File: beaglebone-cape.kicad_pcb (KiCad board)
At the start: 2 copper layers, 86.4 x 54.6 mm, 9 parts, among them J1 CONN_2X2, P1 BEAGLEBONE_BLACK, U1 24C16

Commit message: Ironed out footprints with Rob, started placing stuff
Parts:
- added C2: 10 uF (25V), Capacitors_ThroughHole:C_Radial_D5_L6_P2.5, F.Cu at (166.4, 123.2)
- added C3: 22 uF (16V), Capacitors_ThroughHole:C_Radial_D5_L6_P2.5, F.Cu at (144.8, 124.5)
- added D1: PWR +12V, LEDs:LED-3MM, F.Cu at (222.9, 214.1)
- added D2: PWR +5V, LEDs:LED-3MM, F.Cu at (255.3, 204.5)
- added D3: RED, LEDs:LED-3MM, F.Cu at (230.1, 171.1)
- added D4: GREEN, LEDs:LED-3MM, F.Cu at (226.1, 130.8)
- added D5: RELAY ON, LEDs:LED-3MM, F.Cu at (184.1, 266.7)
- added D6: RELAY ON, LEDs:LED-3MM, F.Cu at (202.3, 258.5)
- added D7: 1N4007, Diodes_ThroughHole:Diode_DO-41_SOD81_Horizontal_RM10, F.Cu at (139.7, 102.9)
- added D8: 1N4007, Diodes_ThroughHole:Diode_DO-41_SOD81_Horizontal_RM10, F.Cu at (139.7, 116.8)
- added D9: 1N4007, Diodes_ThroughHole:Diode_DO-41_SOD81_Horizontal_RM10, F.Cu at (200.8, 225.9)
- added P2: 12V, Terminal_Blocks:TerminalBlock_Pheonix_MPT-2.54mm_2pol, F.Cu at (190.5, 109.2)
- added P3: RED_LIGHT, Terminal_Blocks:TerminalBlock_Pheonix_MPT-2.54mm_2pol, F.Cu at (190.5, 96.5)
- added P4: JUMPERS, Pin_Headers:Pin_Header_Straight_2x02, F.Cu at (176.8, 210.2)
- added P5: GREEN_LIGHT, Terminal_Blocks:TerminalBlock_Pheonix_MPT-2.54mm_2pol, F.Cu at (190.5, 90.2)
- added P6: CONN_01X05, Pin_Headers:Pin_Header_Straight_1x05, F.Cu at (119.4, 105.4)
- added P7: NC/NO JUMPER, Pin_Headers:Pin_Header_Straight_1x03, F.Cu at (179.1, 105.4)
- added P8: NC/NO JUMPER, Pin_Headers:Pin_Header_Straight_1x03, F.Cu at (184.2, 109.2)
- added P9: DOOR STRIKE/MAGNET, Terminal_Blocks:TerminalBlock_Pheonix_MPT-2.54mm_2pol, F.Cu at (190.5, 102.9)
- added Q1: 2N7000, TO_SOT_Packages_THT:TO-92_Inline_Narrow_Oval, F.Cu at (248.2, 190.9)
- added Q2: 2N7000, TO_SOT_Packages_THT:TO-92_Inline_Narrow_Oval, F.Cu at (239.1, 184.8)
- added Q3: 2N7000, TO_SOT_Packages_THT:TO-92_Inline_Narrow_Oval, F.Cu at (216.3, 246.2)
- added Q4: 2N7000, TO_SOT_Packages_THT:TO-92_Inline_Narrow_Oval, F.Cu at (195.4, 259.6)
- added R10: 1k, Resistors_ThroughHole:Resistor_Vertical_RM5mm, F.Cu at (230.9, 194.8)
- added R11: 330, Resistors_ThroughHole:Resistor_Vertical_RM5mm, F.Cu at (196.4, 208.4)
- added R12: 10k, Resistors_ThroughHole:Resistor_Vertical_RM5mm, F.Cu at (186.6, 208.4)
- added R13: 1k, Resistors_ThroughHole:Resistor_Vertical_RM5mm, F.Cu at (241.1, 164.2)
- added R14: 330, Resistors_ThroughHole:Resistor_Vertical_RM5mm, F.Cu at (187.8, 247.2)
- added R15: 330, Resistors_ThroughHole:Resistor_Vertical_RM5mm, F.Cu at (177.0, 259.2)
- added R16: 330, Resistors_ThroughHole:Resistor_Vertical_RM5mm, F.Cu at (167.3, 259.2)
- added R17: 330, Resistors_ThroughHole:Resistor_Vertical_RM5mm, F.Cu at (217.5, 225.6)
- added R18: 10k, Resistors_ThroughHole:Resistor_Vertical_RM5mm, F.Cu at (197.5, 248.9)
- added R19: 10k, Resistors_ThroughHole:Resistor_Vertical_RM5mm, F.Cu at (208.7, 235.6)
- added R20: 1k, Resistors_ThroughHole:Resistor_Vertical_RM5mm, F.Cu at (218.4, 235.6)
- added R21: 1k, Resistors_ThroughHole:Resistor_Vertical_RM5mm, F.Cu at (208.7, 245.5)
- added R22: 2k, Resistors_ThroughHole:Resistor_Vertical_RM5mm, F.Cu at (198.9, 239.0)
- added R23: 2k, Resistors_ThroughHole:Resistor_Vertical_RM5mm, F.Cu at (187.8, 257.2)
- added R6: 1k, Resistors_ThroughHole:Resistor_Vertical_RM5mm, F.Cu at (241.2, 174.1)
- added R7: 330, Resistors_ThroughHole:Resistor_Vertical_RM5mm, F.Cu at (250.9, 160.6)
- added R8: 330, Resistors_ThroughHole:Resistor_Vertical_RM5mm, F.Cu at (250.9, 170.5)
- added R9: 10k, Resistors_ThroughHole:Resistor_Vertical_RM5mm, F.Cu at (206.1, 208.4)
- added RLY1: JW2SN-DC5V, panasonic_jw:Panasonic_JW, F.Cu at (158.8, 97.8)
- added RLY2: JW2SN-DC5V, panasonic_jw:Panasonic_JW, F.Cu at (158.8, 111.8)
- added SW1: PWR_SWITCH, Buttons_Switches_ThroughHole:SW_PUSH_SMALL, F.Cu at (100.3, 97.8)
- added SW2: RESET_SWITCH, Buttons_Switches_ThroughHole:SW_PUSH_SMALL, F.Cu at (100.3, 90.2)
- added U2: V7805-2000, V78XX:V78XX, F.Cu at (156.2, 125.7)
- added U3: 4N25, Housings_DIP:DIP-6_W7.62mm, F.Cu at (137.2, 100.3)
- added U4: 4N25, Housings_DIP:DIP-6_W7.62mm, F.Cu at (137.2, 113.0)
- C1: value 0.1u -> 0.1uF (25V); footprint SM0805 -> Capacitors_ThroughHole:C_Radial_D5_L6_P2.5
- P1: footprint BEAGLEBONE_BLACK -> beagleboard:BEAGLEBONE_BLACK
- R1, R2, R3: footprint SM0805 -> Resistors_ThroughHole:Resistor_Vertical_RM5mm
- R4, R5: value 1.5k -> 5.6k; footprint SM0805 -> Resistors_ThroughHole:Resistor_Vertical_RM5mm
- U1: value 24C16 -> 24C256; footprint SO8E -> Housings_DIP:DIP-8_W7.62mm
- moved R3 158.8 mm to (259.0, 168.6)
- moved R4 154.6 mm to (259.5, 161.5)
- moved R2 153.3 mm to (256.0, 168.6)
- moved R5 149.1 mm to (256.4, 161.5)
- moved C1 129.2 mm to (227.4, 173.1)
- moved J1 111.8 mm to (212.1, 129.5)
- moved R1 96.0 mm to (156.8, 214.6)
- moved U1 4.45 mm to (100.3, 128.3), turned to 90 degrees
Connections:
- net /DC_3.3V renamed +3V3
- net /VDD_5V renamed +5V
- P1 pad A10: (no net) -> /GPIO_68
- P1 pad A11: (no net) -> /GPIO_45
- P1 pad A12: (no net) -> /GPIO_44
- P1 pad A13: (no net) -> /EHRPWM2B
- P1 pad A14: (no net) -> /GPIO_26
- P1 pad A15: (no net) -> /LOCK_RELAYS/R1_ENGAGE
- P1 pad A16: (no net) -> /LOCK_RELAYS/R1_READ
- P1 pad A17: (no net) -> /LOCK_RELAYS/R2_ENGAGE
- P1 pad A18: (no net) -> /LOCK_RELAYS/R2_READ
- P1 pad A19: (no net) -> /EHRPWM2A
- P1 pad A20: (no net) -> /MMC1_CMD
- P1 pad A21: (no net) -> /MMC1_CLK
- P1 pad A22: (no net) -> /MMC1_DAT5
- P1 pad A23: (no net) -> /MMC1_DAT4
- P1 pad A24: (no net) -> /MMC1_DAT1
- P1 pad A25: (no net) -> /MMC1_DAT0
- P1 pad A26: (no net) -> /GPIO_61
- P1 pad A27: (no net) -> /LCD_VSYNC
- P1 pad A28: (no net) -> /LCD_PCLK
- P1 pad A29: (no net) -> /LCD_HSYNC
- P1 pad A3: (no net) -> /MMC1_DAT6
- P1 pad A30: (no net) -> /LCD_AC_BIAS
- P1 pad A31: (no net) -> /LCD_DATA14
- P1 pad A32: (no net) -> /LCD_DATA15
- P1 pad A33: (no net) -> /LCD_DATA13
- P1 pad A34: (no net) -> /LCD_DATA11
- P1 pad A35: (no net) -> /LCD_DATA12
- P1 pad A36: (no net) -> /LCD_DATA10
- P1 pad A37: (no net) -> /LCD_DATA8
- P1 pad A38: (no net) -> /LCD_DATA9
- P1 pad A39: (no net) -> /LCD_DATA6
- P1 pad A4: (no net) -> /MMC1_DAT7
- P1 pad A40: (no net) -> /LCD_DATA7
- P1 pad A41: (no net) -> /LCD_DATA4
- P1 pad A42: (no net) -> /LCD_DATA5
- P1 pad A43: (no net) -> /LCD_DATA2
- P1 pad A44: (no net) -> /LCD_DATA3
- P1 pad A45: (no net) -> /LCD_DATA0
- P1 pad A46: (no net) -> /LCD_DATA1
- P1 pad A5: (no net) -> /MMC1_DAT2
- P1 pad A6: (no net) -> /MMC1_DAT3
- P1 pad A7: (no net) -> /GPIO_66
- P1 pad A8: (no net) -> /GPIO_67
- P1 pad A9: (no net) -> /GPIO_69
- P1 pad B10: (no net) -> /SYS_RESETn
- P1 pad B11: (no net) -> /UART4_RXD
- P1 pad B12: (no net) -> /GPIO_60
- P1 pad B13: (no net) -> /UART4_TXD
- P1 pad B14: (no net) -> /EHRPWM1A
- P1 pad B15: (no net) -> /GPIO_48
- P1 pad B16: (no net) -> /EHRPWM1B
- P1 pad B17: (no net) -> /SPIO_CSO
- P1 pad B18: (no net) -> /SPIO_D1
- P1 pad B21: (no net) -> /SPIO_DO
- P1 pad B22: (no net) -> /SPIO_SLCK
- P1 pad B23: (no net) -> /GPIO_49
- P1 pad B24: (no net) -> /UART1_TXD
- P1 pad B25: (no net) -> /GPIO_117
- P1 pad B26: (no net) -> /UART1_RXD
- P1 pad B27: (no net) -> /GPIO_115
- P1 pad B28: (no net) -> /SPI1_CS0
- P1 pad B29: (no net) -> /SPI1_D0
- P1 pad B30: (no net) -> /GPIO_112
- P1 pad B31: (no net) -> /SPI1_SCLK
- P1 pad B32: (no net) -> /VADC
- P1 pad B33: (no net) -> /AIN4
- P1 pad B34: (no net) -> /AGND
- P1 pad B35: (no net) -> /AIN6
- P1 pad B36: (no net) -> /AIN5
- P1 pad B37: (no net) -> /AIN2
- P1 pad B38: (no net) -> /AIN3
- P1 pad B39: (no net) -> /AIN0
- P1 pad B40: (no net) -> /AIN1
- P1 pad B41: (no net) -> /GPIO_20
- P1 pad B42: (no net) -> /ECAPWMO
- P1 pad B9: (no net) -> /PWR_BUT
- U1 pad 7: (no net) -> Net-(U1-Pad7)
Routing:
- net (no net): track 0.00 -> 51.8 mm, vias 0 -> 2
- net /A0: track 15.6 -> 0.00 mm
- net +3V3: track 43.4 -> 31.1 mm
- net /A2: track 11.2 -> 0.00 mm
- net /A1: track 10.1 -> 0.00 mm
- net GND: track 2.60 -> 0.00 mm, vias 2 -> 0

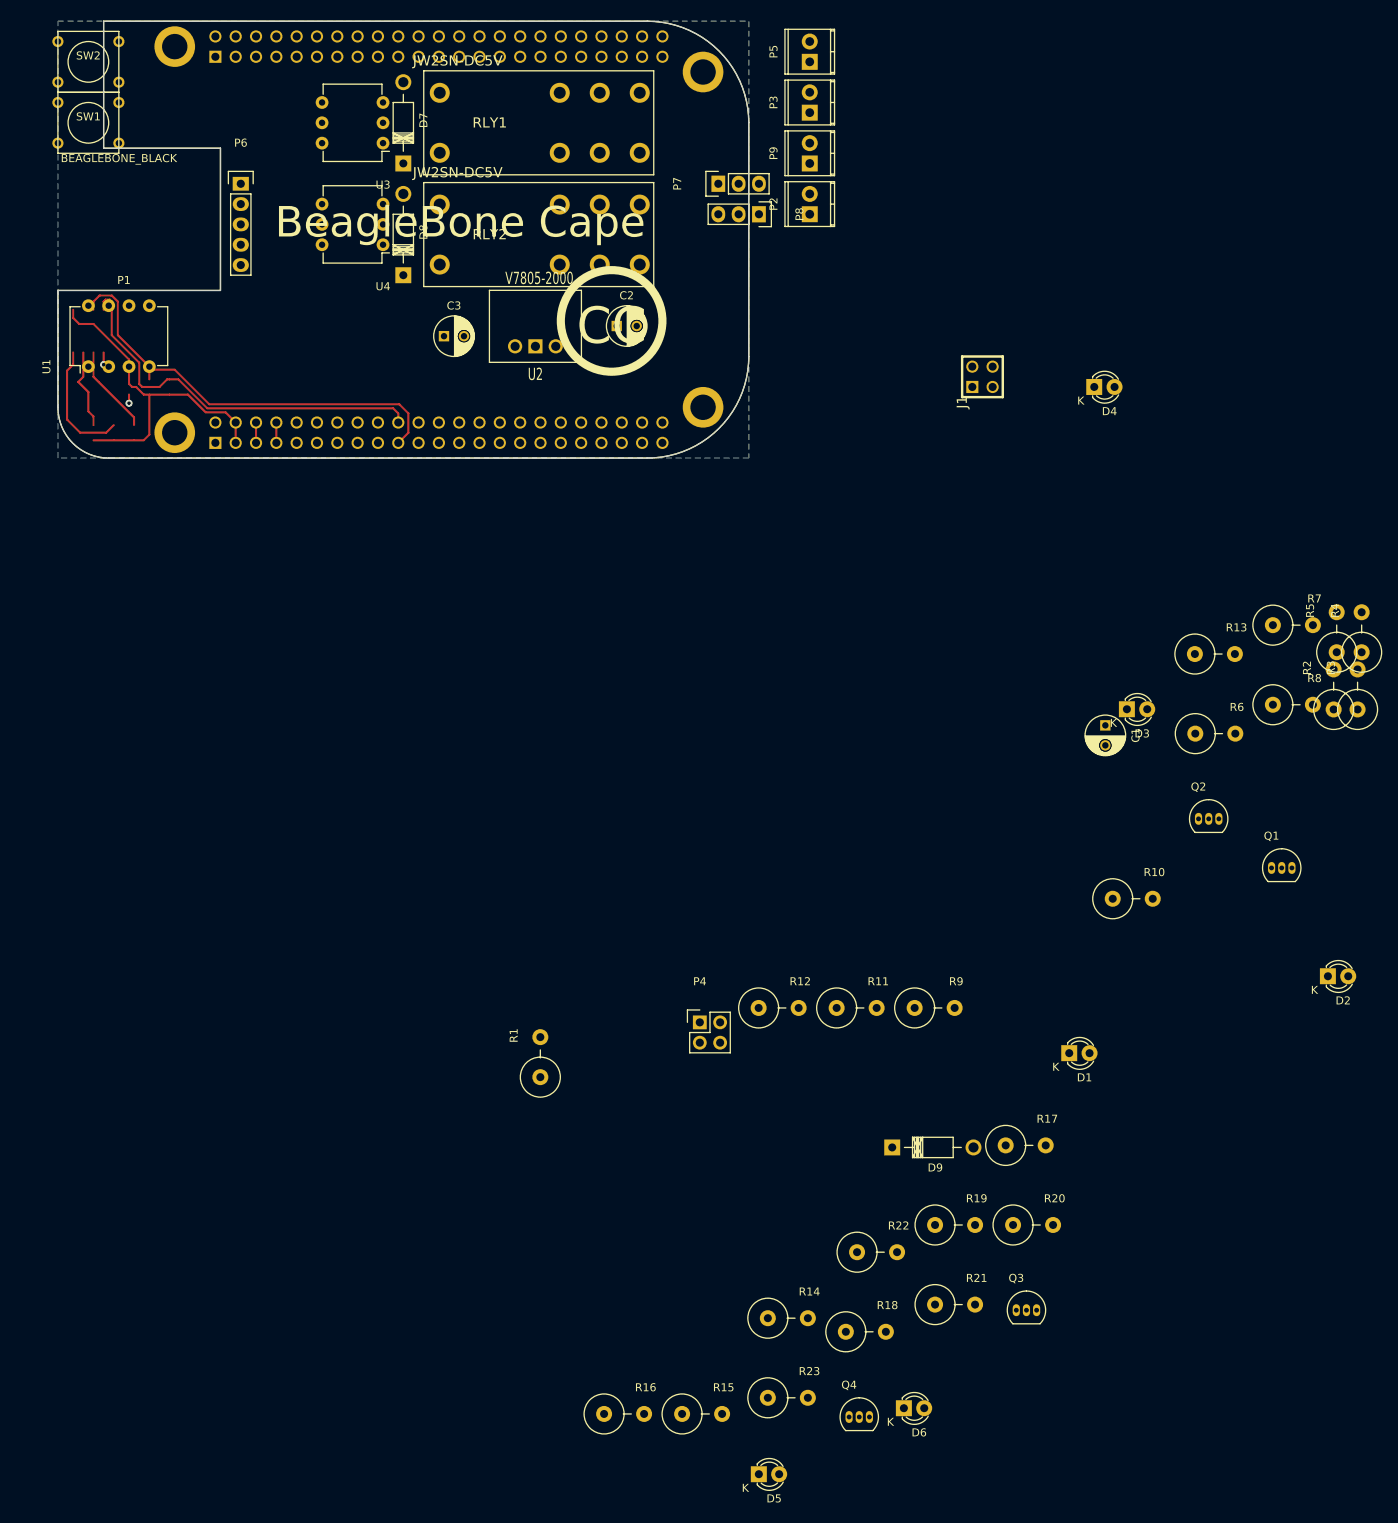
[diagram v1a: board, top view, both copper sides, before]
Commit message: Moved a bunch of footprints around
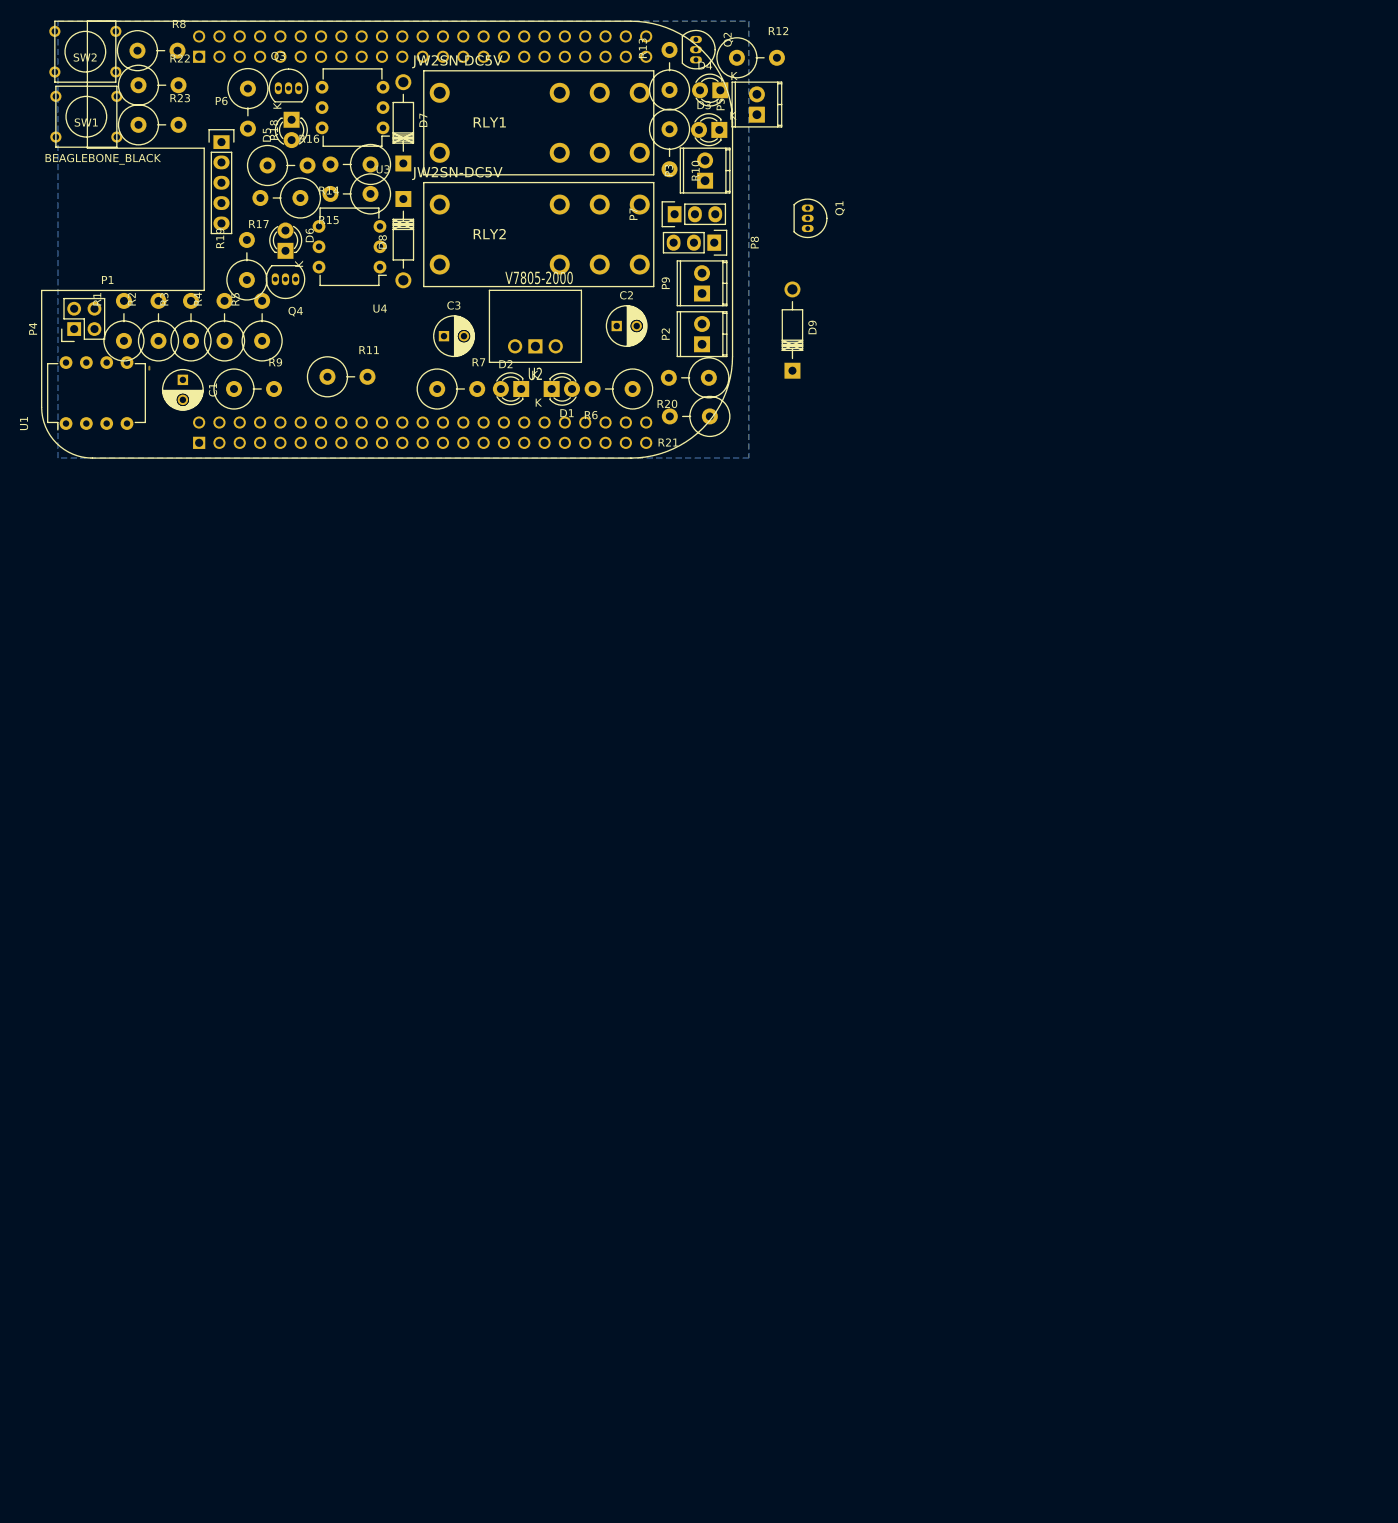
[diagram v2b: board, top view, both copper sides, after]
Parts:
- removed J1: CONN_2X2, PIN_ARRAY_2X2
- P1: footprint beagleboard:BEAGLEBONE_BLACK -> beagleboard.new:BEAGLEBONE_BLACK
- moved D5 179.1 mm to (125.7, 97.4), turned to 270 degrees
- moved Q3 178.4 mm to (124.1, 93.5)
- moved R23 177.5 mm to (109.1, 98.0)
- moved R22 171.3 mm to (109.1, 93.1)
- moved R18 171.3 mm to (120.3, 96.0), turned to 270 degrees
- moved D6 164.0 mm to (125.0, 113.8), turned to 90 degrees
- moved R8 163.8 mm to (109.0, 88.8)
- moved R16 161.6 mm to (125.2, 103.1)
- moved R15 158.7 mm to (133.1, 106.7), turned to 180 degrees
- moved Q4 158.1 mm to (126.2, 117.3), turned to 180 degrees
- moved R14 154.2 mm to (133.1, 103.0), turned to 180 degrees
- moved R2 153.9 mm to (109.1, 122.6)
- moved R3 152.9 mm to (113.2, 122.6)
- moved R17 150.7 mm to (124.3, 107.2), turned to 180 degrees
- moved R19 149.6 mm to (120.1, 114.9), turned to 90 degrees
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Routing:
- net /I2C2_SCL: track 54.9 -> 0.00 mm
- net (no net): track 51.8 -> 0.38 mm, vias 2 -> 0
- net /I2C2_SDA: track 49.8 -> 0.00 mm
- net +3V3: track 31.1 -> 0.00 mm
- net /SYS_5V: track 2.54 -> 0.00 mm
- net +5V: track 2.54 -> 0.00 mm
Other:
- board outline removed
- board text removed: "BeagleBone Cape"
- board text removed: "CC"

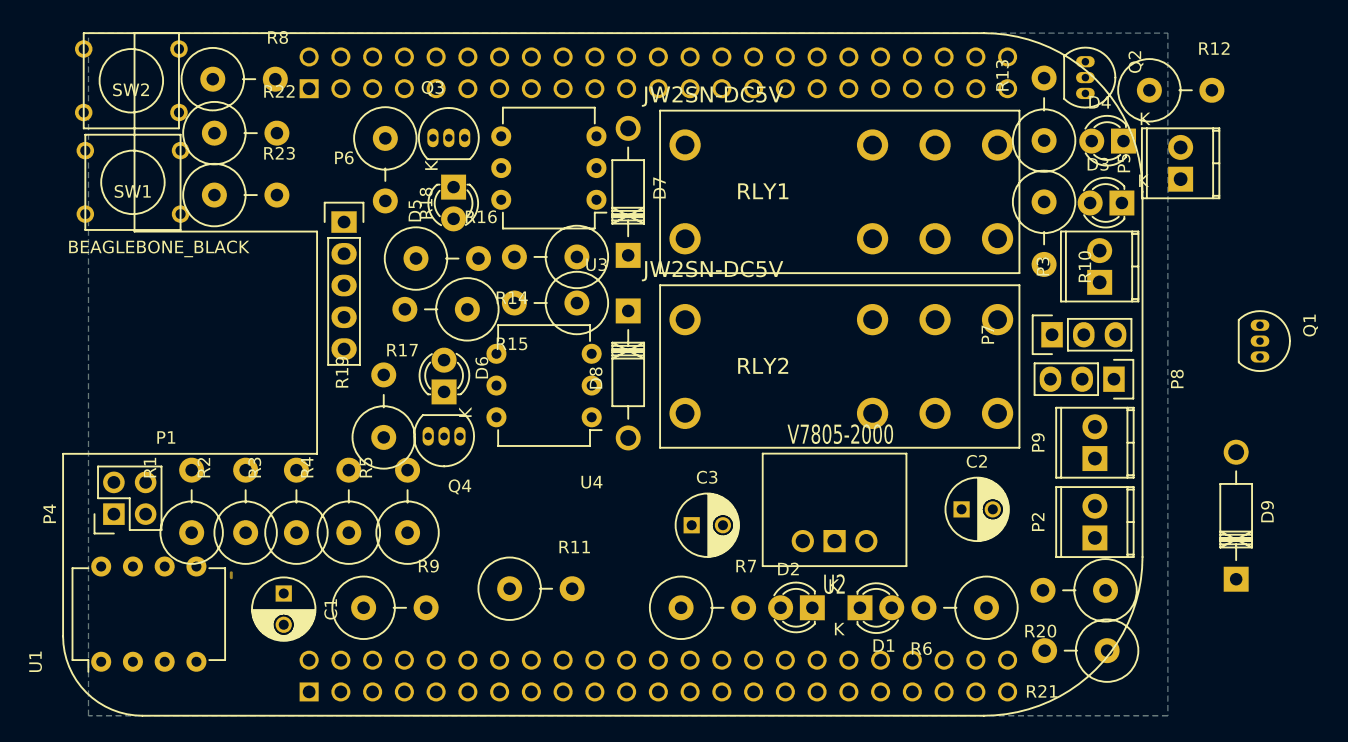
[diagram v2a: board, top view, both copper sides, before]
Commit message: unbelievably managed to squeeze everything on the board
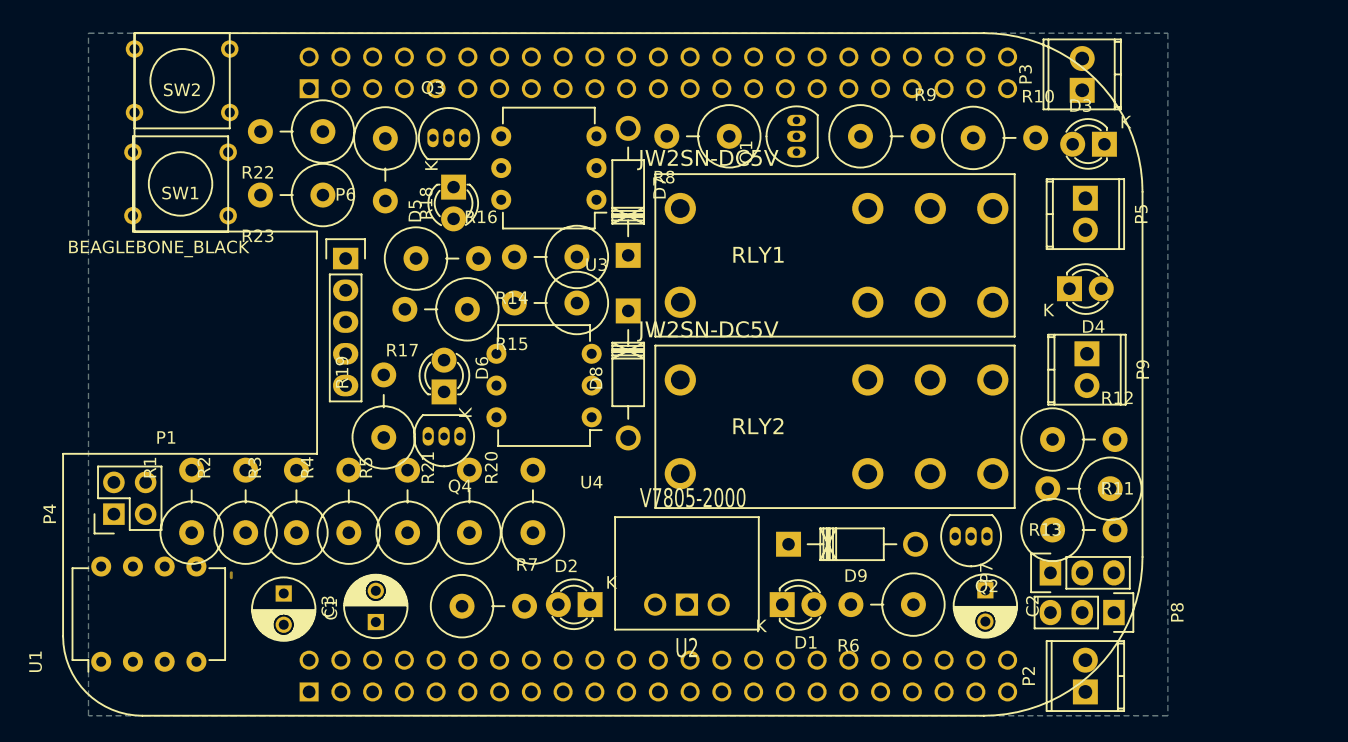
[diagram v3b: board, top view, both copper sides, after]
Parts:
- moved R9 54.8 mm to (160.8, 93.3)
- moved R21 50.0 mm to (127.0, 122.6), turned to 90 degrees
- moved R20 43.9 mm to (132.1, 122.6), turned to 90 degrees
- moved R11 43.7 mm to (176.1, 124.8)
- moved Q1 39.6 mm to (153.2, 94.6), turned to 90 degrees
- moved Q2 38.8 mm to (168.4, 125.3), turned to 180 degrees
- moved R8 36.6 mm to (145.3, 93.3), turned to 180 degrees
- moved D9 35.9 mm to (152.5, 126.0), turned to 0 degrees
- moved R13 30.5 mm to (175.8, 121.5), turned to 180 degrees
- moved R12 29.0 mm to (176.1, 117.6)
- moved C3 26.4 mm to (119.5, 132.2), turned to 90 degrees
- moved P7 19.1 mm to (173.5, 128.3)
- moved P8 18.7 mm to (178.6, 131.4)
- moved D2 17.8 mm to (136.7, 130.8)
- moved R7 17.5 mm to (128.9, 130.9)
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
